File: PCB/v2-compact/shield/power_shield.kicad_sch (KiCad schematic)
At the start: 6 parts, among them U41 AP7361C-3.3

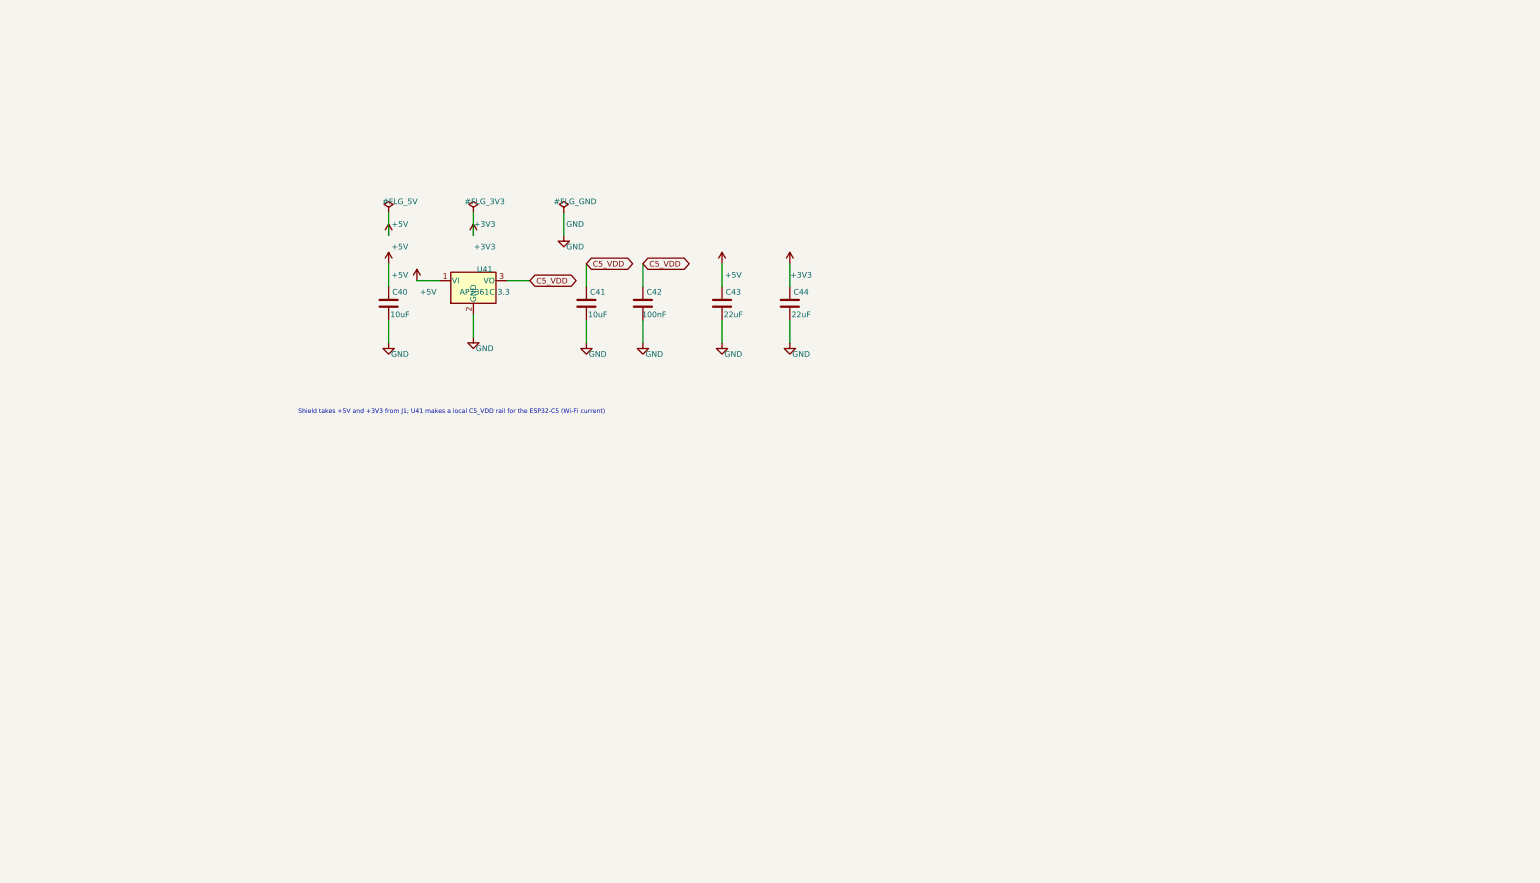
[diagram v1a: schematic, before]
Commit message: Schematic: add battery + USB-C charger power subsystem (BQ25896, 2500mAh)
Adds the full power section to the shield's power sheet, per the battery/stacking research:
- USB-C (J50 VBUS) -> BQ25896 (3A switch-mode charger + power-path + I2C). Charges a 2500mAh
  1S LiPo (BT50, JST-PH) through DW01A/FS8205 protection (U56); MAX17048 fuel gauge (U57).
- Power-path SYS -> TPS63020 buck-boost = system +3V3 (holds regulation as the cell sags),
  and -> TPS61230A boost = system +5V (feeds the RV1106). AP7361C LDO still makes clean C5_VDD.
- Rewired: J50 is now the charge/data input (VBUS), and the RV1106 is powered from the system
  +5V rail instead of being self-powered. +5V/+3V3 distribute to both boards over J1.
- New functional symbols (BQ25896/TPS63020/MAX17048/TPS61230A/DW01) in SnowOwl.kicad_sym.

Verified by KiCad's netlister: GND=79 (top net, intact), VBUS=3, VBAT=6, VSYS=8, +5V=13,
+3V3=36 - all rails distinct, no merges. Fixed two stub-collision shorts found while building
(input cap on the charger's pin column; VBAT power-flag on a cap column) and upgraded
find_shorts.py to catch pin-on-wire collisions, not just endpoint snaps.

FIRST-PASS: IC pinouts + passive values are placeholders to VERIFY vs datasheets. The power
PARTS still need placing on the PCB (next step), and the main board's own USB/LDO reconciled.
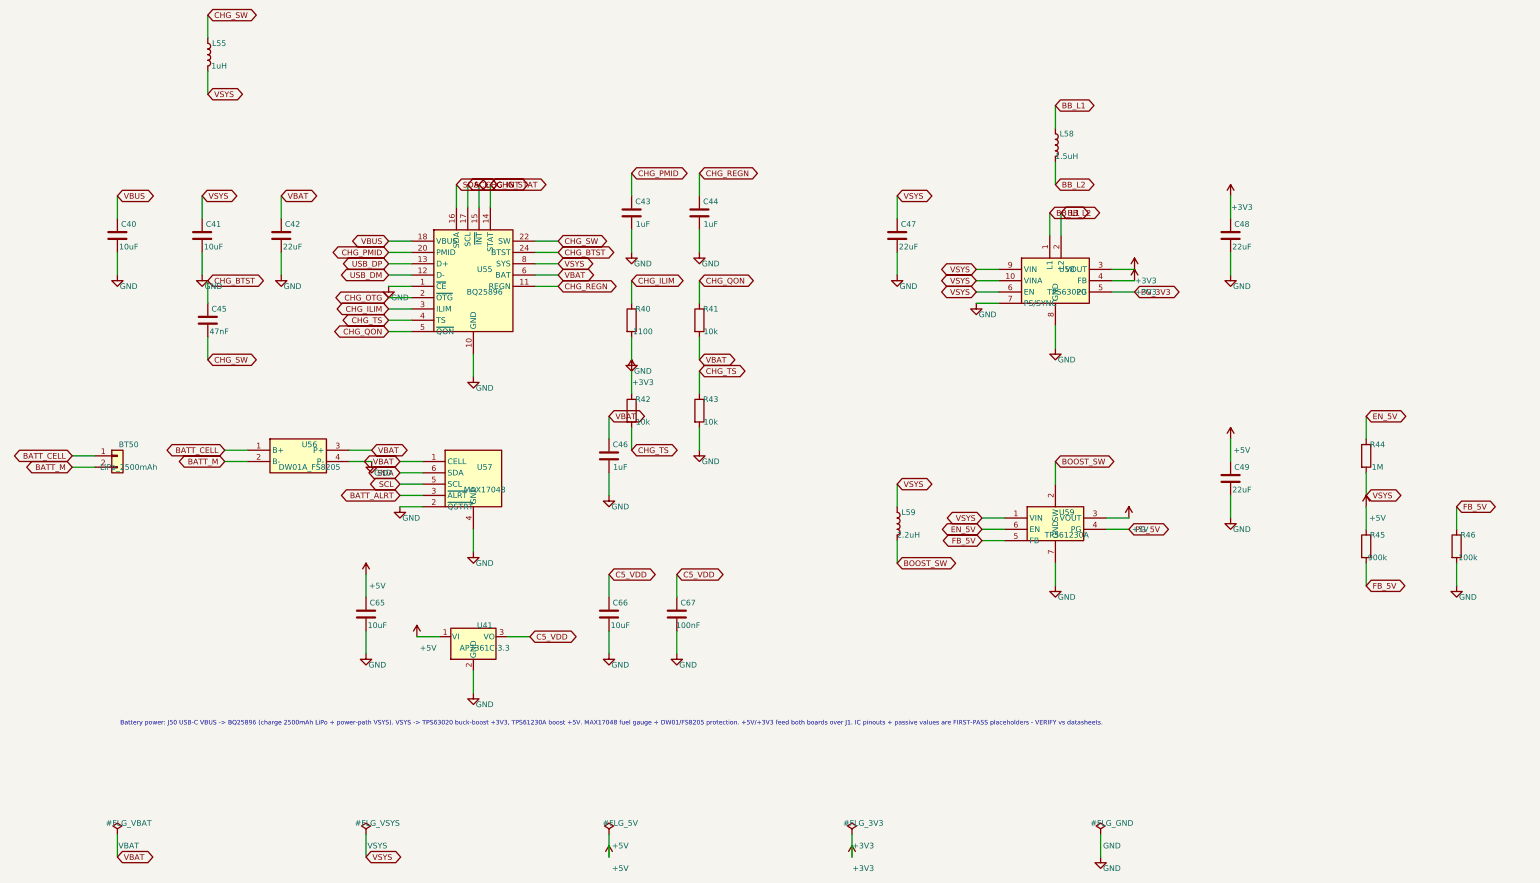
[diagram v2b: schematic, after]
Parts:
- added BT50: LiPo_2500mAh, Connector_JST:JST_PH_S2B-PH-K_1x02_P2.00mm_Horizontal, symbol Connector_Generic:Conn_01x02
- added C45: 47nF, Capacitor_SMD:C_0402_1005Metric, symbol Device:C
- added C46: 1uF, Capacitor_SMD:C_0402_1005Metric, symbol Device:C
- added C47, C48, C49: 22uF, Capacitor_SMD:C_0402_1005Metric, symbol Device:C
- added C65, C66: 10uF, Capacitor_SMD:C_0402_1005Metric, symbol Device:C
- added C67: 100nF, Capacitor_SMD:C_0402_1005Metric, symbol Device:C
- added L55: 1uH, Inductor_SMD:L_1210_3225Metric, symbol Device:L
- added L58: 1.5uH, Inductor_SMD:L_1210_3225Metric, symbol Device:L
- added L59: 2.2uH, Inductor_SMD:L_1210_3225Metric, symbol Device:L
- added R40: 1100, Resistor_SMD:R_0402_1005Metric, symbol Device:R
- added R41, R42, R43: 10k, Resistor_SMD:R_0402_1005Metric, symbol Device:R
- added R44: 1M, Resistor_SMD:R_0402_1005Metric, symbol Device:R
- added R45: 900k, Resistor_SMD:R_0402_1005Metric, symbol Device:R
- added R46: 100k, Resistor_SMD:R_0402_1005Metric, symbol Device:R
- added U55: BQ25896, Package_DFN_QFN:QFN-24-1EP_4x4mm_P0.5mm_EP2.5x2.5mm, symbol SnowOwl:BQ25896
- added U56: DW01A_FS8205, Package_TO_SOT_SMD:SOT-23-6, symbol SnowOwl:BattProtect_DW01
- added U57: MAX17048, Package_DFN_QFN:DFN-8-1EP_2x3mm_P0.5mm_EP0.61x2.2mm, symbol SnowOwl:MAX17048
- added U58: TPS63020, Package_DFN_QFN:DFN-10-1EP_3x3mm_P0.5mm_EP1.58x2.35mm, symbol SnowOwl:TPS63020
- added U59: TPS61230A, Package_DFN_QFN:DFN-10-1EP_3x3mm_P0.5mm_EP1.58x2.35mm, symbol SnowOwl:TPS61230A
- C42: value 100nF -> 22uF
- C43, C44: value 22uF -> 1uF
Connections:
- net +3V3: now also C48.1, R42.1, U58.3 (VOUT), U58.4 (FB); no longer C44.1
- net +5V: now also C49.1, C65.1, R45.1, U59.3 (VOUT); no longer C40.1, C43.1
- net C5_VDD: now also C66.1, C67.1; no longer C41.1, C42.1
- net GND: now also C46.2, C47.2, C48.2, C49.2, C65.2, C66.2, C67.2, R40.2, R43.2, R46.2, U55.1 (~{CE}), U55.10 (GND), U56.4 (P-), U57.2 (~{QSTRT}), U57.4 (GND), U58.7 (PS/SYNC), U58.8 (GND), U59.7 (GND)
- new net BATT_ALRT: U57.3 (~{ALRT})
- new net BATT_CELL: BT50.1 (Pin_1), U56.1 (B+)
- new net BATT_M: BT50.2 (Pin_2), U56.2 (B-)
- new net BB_L1: L58.1, U58.1 (L1)
- new net BB_L2: L58.2, U58.2 (L2)
- new net BOOST_SW: L59.2, U59.2 (SW)
- new net CHG_BTST: C45.1, U55.24 (BTST)
- new net CHG_ILIM: R40.1, U55.3 (ILIM)
- new net CHG_INT: U55.15 (~{INT})
- new net CHG_OTG: U55.2 (~{OTG})
- new net CHG_PMID: C43.1, U55.20 (PMID)
- new net CHG_QON: R41.1, U55.5 (~{QON})
- new net CHG_REGN: C44.1, U55.11 (REGN)
- new net CHG_STAT: U55.14 (STAT)
- new net CHG_SW: C45.2, L55.1, U55.22 (SW)
- new net CHG_TS: R42.2, R43.1, U55.4 (TS)
- new net EN_5V: R44.1, U59.6 (EN)
- new net FB_5V: R45.2, R46.1, U59.5 (FB)
- new net PG_3V3: U58.5 (PG)
- new net PG_5V: U59.4 (PG)
- new net SCL: U55.17 (SCL), U57.5 (SCL)
- new net SDA: U55.16 (SDA), U57.6 (SDA)
- new net USB_DM: U55.12 (D-)
- new net USB_DP: U55.13 (D+)
- new net VBAT: C42.1, C46.1, R41.2, U55.6 (BAT), U56.3 (P+), U57.1 (CELL)
- new net VBUS: C40.1, U55.18 (VBUS)
- new net VSYS: C41.1, C47.1, L55.2, L59.1, R44.2, U55.8 (SYS), U58.10 (VINA), U58.6 (EN), U58.9 (VIN), U59.1 (VIN)
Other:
- note added: "Battery power: J50 USB-C VBUS -> BQ25896 (charge 2500mAh LiPo + power-path VSYS). VSYS -> TPS63020 buck-boost +3V3, TPS61230A boost +5V. MAX17048 fuel gauge + DW01/FS8205 protection. +5V/+3V3 feed both boards over J1. IC pinouts + passive values are FIRST-PASS placeholders - VERIFY vs datasheets."
- note removed: "Shield takes +5V and +3V3 from J1; U41 makes a local C5_VDD rail for the ESP32-C5 (Wi-Fi current)"

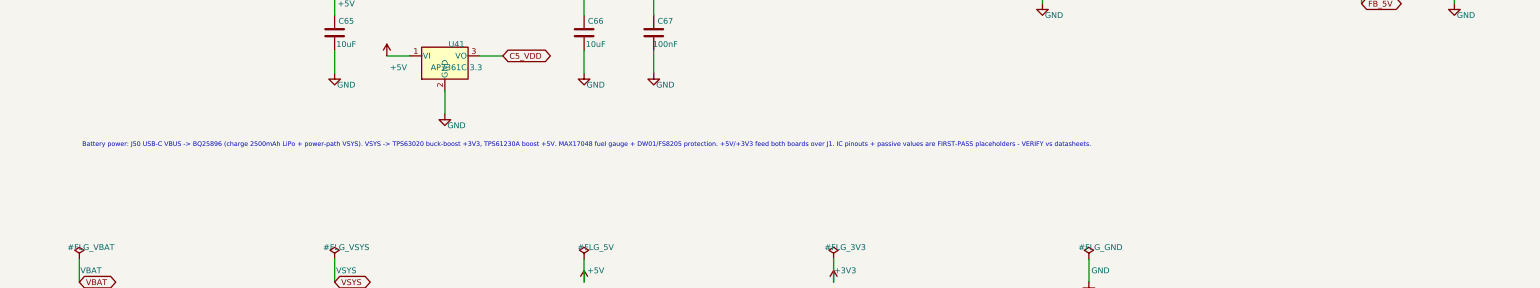
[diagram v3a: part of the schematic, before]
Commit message: Single USB-C + battery power; J1 vertical on the left edge; U30 model; back-side comments
Power/architecture:
- Remove J50 (the RV1106's own USB-C). The device now has ONE USB-C: the main board's J20.
  J20's VBUS is carried over J1 pin19 (was SPARE) to the shield's BQ25896 charger, so charging +
  the ESP32-S3 data/programming share the single port. Everything runs off the battery.
- Reconcile the nets: J20 VBUS -> VBUS (was VBUS_MAIN), charger VBUS <- J1 pin19, RV1106 keeps its
  microSD (J51) but loses its USB port (reached over UART on J1). Removed orphans R95/R96 (J50 CC
  resistors) and the redundant main LDO U21. Verified: J1 mates 20/20 on both boards, VBUS spans
  J20 -> J1 -> U55, GND healthy (106/37 nodes), no bad net merges.

Placement:
- J1 stack header: was horizontal mid-board, now VERTICAL on the WEST edge at the same spot on both
  boards (they still mate). Nudged the shield's PN532/flash/HTRC (U7/U12/U8) east to clear it, and
  the main's screen east. Status LEDs D10/D11 pulled off the corner mounting holes. 0 real overlaps.

3D + silk:
- U30 (RV1106 Core1106): no KiCad model exists for the Luckfox SoM -> add a sized VRML module
  stand-in (SnowOwl.3dshapes/RV1106_Core1106.wrl; sizes pre-divided by 2.54 for KiCad's inch-unit
  VRML reader). USB-C model: swap the vertical USB4085 for the 16-pin horizontal USB4105 so it
  seats correctly against the horizontal HRO footprint.
- ESP32-BlackRaven art: logo moved to the top by the LEDs, raven dropped down to fill the board.
  Dropped the cluttering TFT label (fab outline kept). Added five back-side silkscreen comments on
  the main board (title/rev, battery, power path, USB-C role, J1 purpose).

Deferred (SWIG pcbnew geometry calls are failing in this environment right now): re-pour the inner
GND/+3V3 planes (inner layers, not visible in renders); apply the datasheet pinout/value fixes to
the power ICs (BQ25896/TPS63020/TPS61230A/MAX17048).
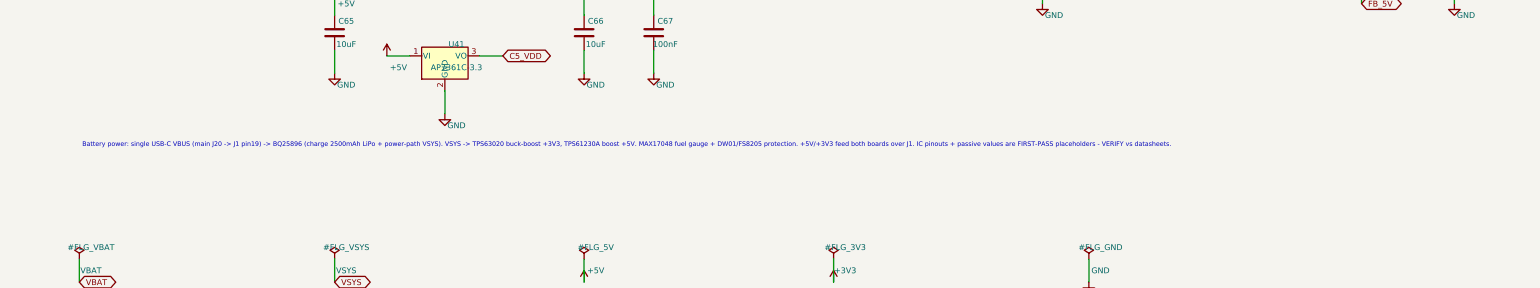
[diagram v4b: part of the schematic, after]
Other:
- note added: "Battery power: single USB-C VBUS (main J20 -> J1 pin19) -> BQ25896 (charge 2500mAh LiPo + power-path VSYS). VSYS -> TPS63020 buck-boost +3V3, TPS61230A boost +5V. MAX17048 fuel gauge + DW01/FS8205 protection. +5V/+3V3 feed both boards over J1. IC pinouts + passive values are FIRST-PASS placeholders - VERIFY vs datasheets."
- note removed: "Battery power: J50 USB-C VBUS -> BQ25896 (charge 2500mAh LiPo + power-path VSYS). VSYS -> TPS63020 buck-boost +3V3, TPS61230A boost +5V. MAX17048 fuel gauge + DW01/FS8205 protection. +5V/+3V3 feed both boards over J1. IC pinouts + passive values are FIRST-PASS placeholders - VERIFY vs datasheets."
